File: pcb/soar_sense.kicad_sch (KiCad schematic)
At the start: 39 parts, among them J1 Conn_02x03_Top_Bottom, J2 Conn_02x02_Top_Bottom, J3 Conn_02x02_Top_Bottom, J4 Conn_02x02_Top_Bottom, J5 Conn_02x02_Top_Bottom, J6 Conn_02x01, J7 Conn_02x03_Top_Bottom, J8 Conn_02x04_Top_Bottom, U1 SPX3819M5-L-3-3, U2 STM32F103CBTx, U3 SHT35-DIS, U4 MAX3051, Y1 8MHz

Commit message: today done
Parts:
- removed J2: Conn_02x02_Top_Bottom, OWN_Parts:pcb_edge_2_2, symbol Connector_Generic:Conn_02x02_Top_Bottom
- added C15, C16, C17, C18, C19, C20: 100n, Capacitor_SMD:C_0603_1608Metric, symbol Device:C_Small
- added D10, D11, D12, D5, D6, D7, D8, D9: D_TVS, Diode_SMD:D_SOD-323, symbol Device:D_TVS
- added JP1: SolderJumper_2_Open, Jumper:SolderJumper-2_P1.3mm_Open_Pad1.0x1.5mm, symbol Jumper:SolderJumper_2_Open
- added R10, R11, R12, R13, R14, R15, R9: 10k, Resistor_SMD:R_0603_1608Metric, symbol Device:R_Small
- C10, C11, C12, C13, C14, C2, C6, C8, C9: LCSC Part Number (none) -> C14663
- C4: LCSC Part Number (none) -> C57112
- FB1: LCSC Part Number (none) -> C1017
- R1: LCSC Part Number (none) -> C25804
- R2: value 100k -> 120R; LCSC Part Number (none) -> C22787
- R4: value 100k -> 10k
- R5, R6: LCSC Part Number (none) -> C23162
- Y1: footprint (none) -> Crystal:Crystal_SMD_3225-4Pin_3.2x2.5mm
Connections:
- net +3V3: now also J1.2 (Pin_2), J1.3 (Pin_3); no longer J1.5 (Pin_5), J1.6 (Pin_6)
- net ADC_IN0: now also C19.1, R15.2; no longer J8.8 (Pin_8)
- net ADC_IN1: now also C16.1, R13.2; no longer J8.7 (Pin_7)
- net ADC_IN2: now also C17.1, R14.2; no longer J8.6 (Pin_6)
- net ADC_IN3: now also C15.1, R12.2; no longer J8.5 (Pin_5)
- net ADC_IN4: now also R4.2, C18.1; no longer J8.4 (Pin_4)
- net BOOT0: now also J1.1 (Pin_1), U2.44 (BOOT0), R9.2; no longer J1.3 (Pin_3), R4.2
- net BOOT1: now also U2.20 (PB2), R10.2; no longer J1.4 (Pin_4), R2.2
- net CAN_H: now also R2.1
- net CAN_L: now also JP1.2 (B)
- net GND: now also J1.4 (Pin_4), C15.2, C16.2, C17.2, C18.2, C19.2, C20.2, D10.1 (A1), D11.1 (A1), D12.1 (A1), D5.1 (A1), D6.1 (A1), D7.1 (A1), D8.1 (A1), D9.1 (A1), R10.1, R9.1; no longer J1.1 (Pin_1), J1.2 (Pin_2)
- net I2C1_SCL: now also D12.2 (A2)
- net I2C1_SDA: now also D11.2 (A2)
- net I2C2_SCL: now also D9.2 (A2)
- net I2C2_SDA: now also D10.2 (A2)
- net SPI2_MISO: now also D8.2 (A2)
- net SPI2_MOSI: now also D7.2 (A2)
- net SPI2_NSS: now also D5.2 (A2)
- net SPI2_SCK: now also D6.2 (A2)
- net USART1_RX: now also J1.5 (Pin_5)
- net USART1_TX: now also J1.6 (Pin_6)
- net VIN: now also D3.2 (A)
- net ADC_INPUT4: now reaches R4.1
- net ADC_INPUT4: now also J8.4 (Pin_4); no longer U2.44 (BOOT0)
- net ADC_INPUT5: now reaches J8.3 (Pin_3)
- net ADC_INPUT5: now also R11.1
- net ADC_IN5: now reaches U2.15 (PA5)
- net ADC_IN5: now also C20.1, R11.2
- new net: JP1.1 (A), R2.2
- new net ADC_INPUT0: J8.8 (Pin_8), R15.1
- new net ADC_INPUT1: J8.7 (Pin_7), R13.1
- new net ADC_INPUT2: J8.6 (Pin_6), R14.1
- new net ADC_INPUT3: J8.5 (Pin_5), R12.1
- no-connect marks 4 -> 15
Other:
- note added: "only overvoltage protection for adcs."
- note removed: "Input Protection"
- moved on the sheet: C14, J1, J3, J4, J5, J8, U4

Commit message: added crystal
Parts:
- removed R3: ??Ohm, Resistor_SMD:R_0603_1608Metric, symbol Device:R_Small
- C3, C5: value ??pF -> 30p; footprint Capacitor_SMD:C_0603_1608Metric -> Capacitor_SMD:C_0402_1005Metric; LCSC Part Number (none) -> C1570
- Y1: footprint Crystal:Crystal_SMD_3225-4Pin_3.2x2.5mm -> Crystal:Crystal_SMD_5032-4Pin_5.0x3.2mm; LCSC Part Number (none) -> C157341
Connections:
- net at C5.1, Y1.3: now also U2.6 (PD1)
- no-connect marks 15 -> 13
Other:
- note added: "CL = 2 * (Cload - Cstray)"
- moved on the sheet: C3, C5, Y1

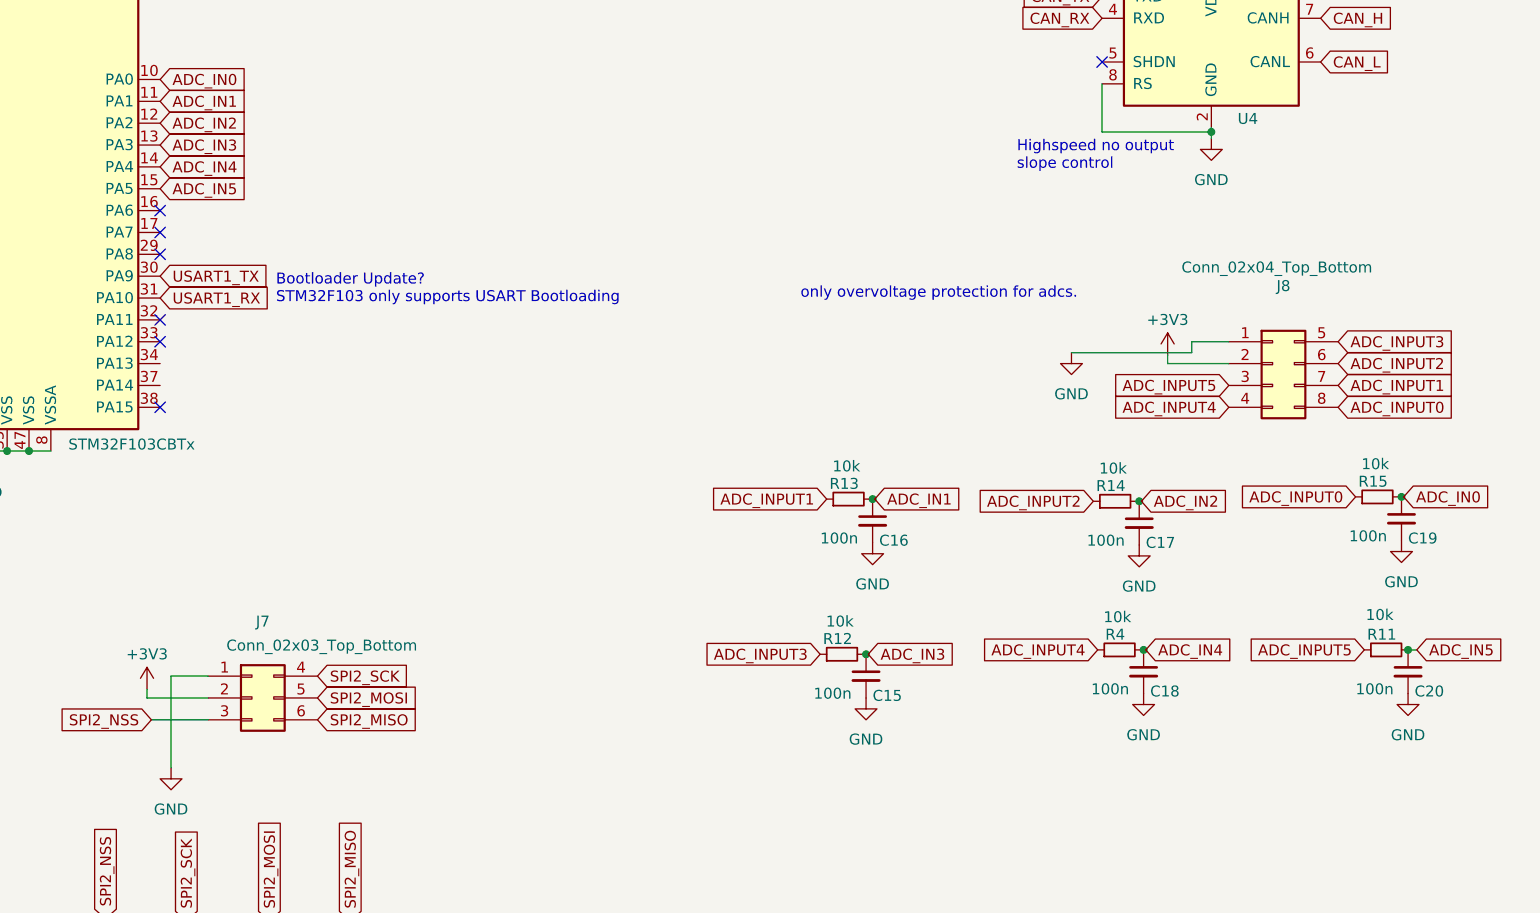
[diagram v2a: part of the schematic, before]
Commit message: sht connected
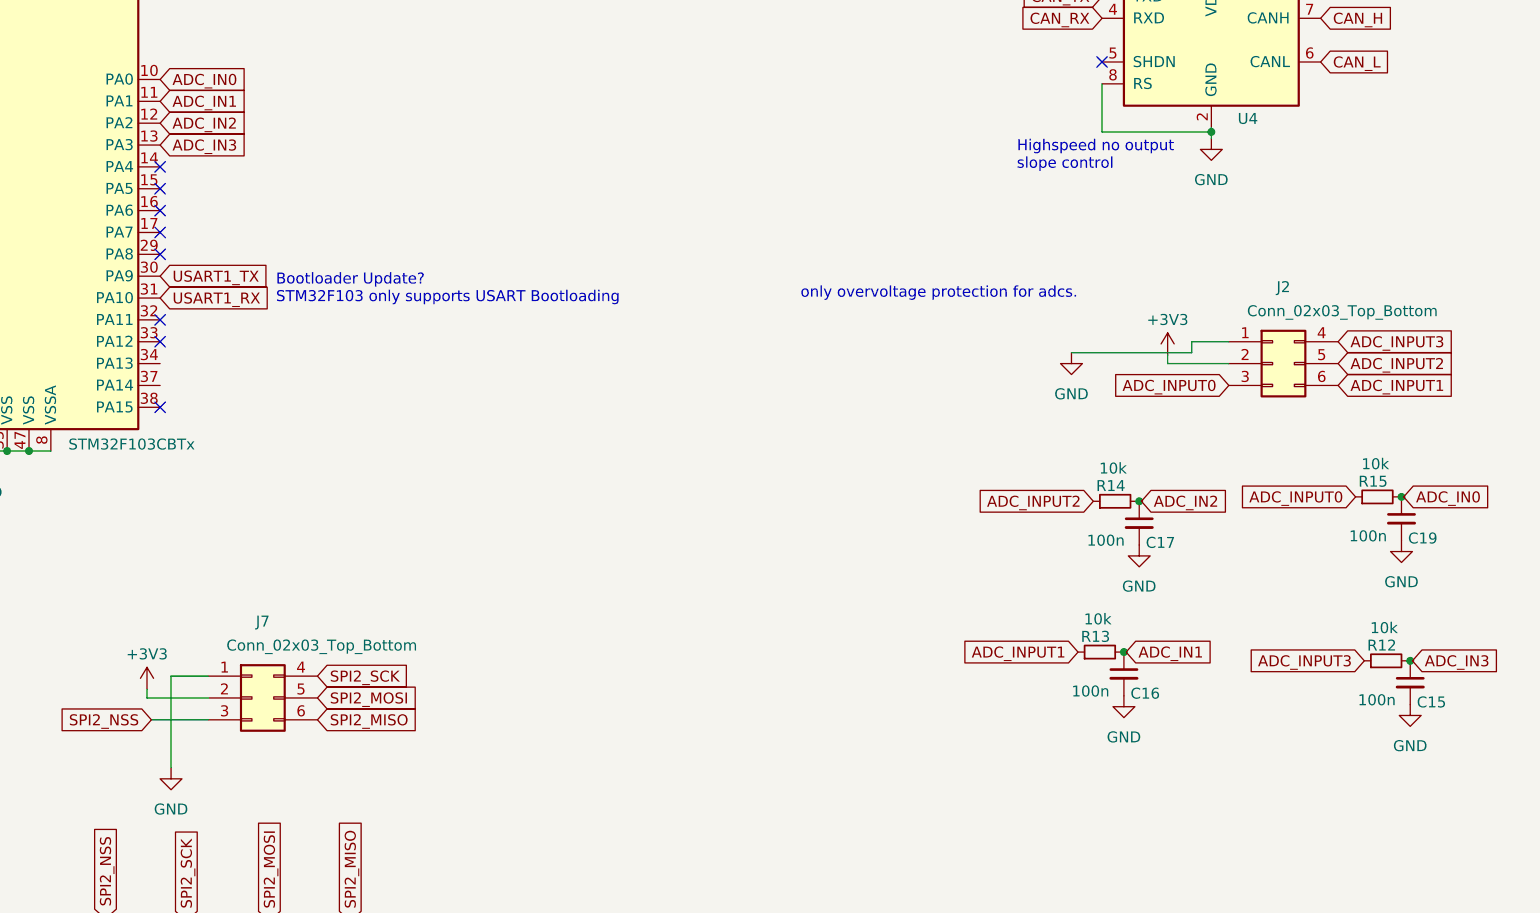
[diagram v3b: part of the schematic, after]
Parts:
- removed C18, C20: 100n, Capacitor_SMD:C_0603_1608Metric, symbol Device:C_Small
- removed J8: Conn_02x04_Top_Bottom, OWN_Parts:pcb_edge_2_4, symbol Connector_Generic:Conn_02x04_Top_Bottom
- removed R11, R4: 10k, Resistor_SMD:R_0603_1608Metric, symbol Device:R_Small
- added J2: Conn_02x03_Top_Bottom, OWN_Parts:pcb_edge_2_3, symbol Connector_Generic:Conn_02x03_Top_Bottom
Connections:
- net +3V3: now also J2.2 (Pin_2)
- net ADC_INPUT0: now also J2.3 (Pin_3)
- net ADC_INPUT1: now also J2.6 (Pin_6)
- net ADC_INPUT2: now also J2.5 (Pin_5)
- net ADC_INPUT3: now also J2.4 (Pin_4)
- net GND: now also J2.1 (Pin_1)
- net ADC_IN4: no longer names the net of U2.14 (PA4)
- net ADC_IN5: no longer names the net of U2.15 (PA5)
- no-connect marks 13 -> 15
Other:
- moved on the sheet: C15, C16, R12, R13

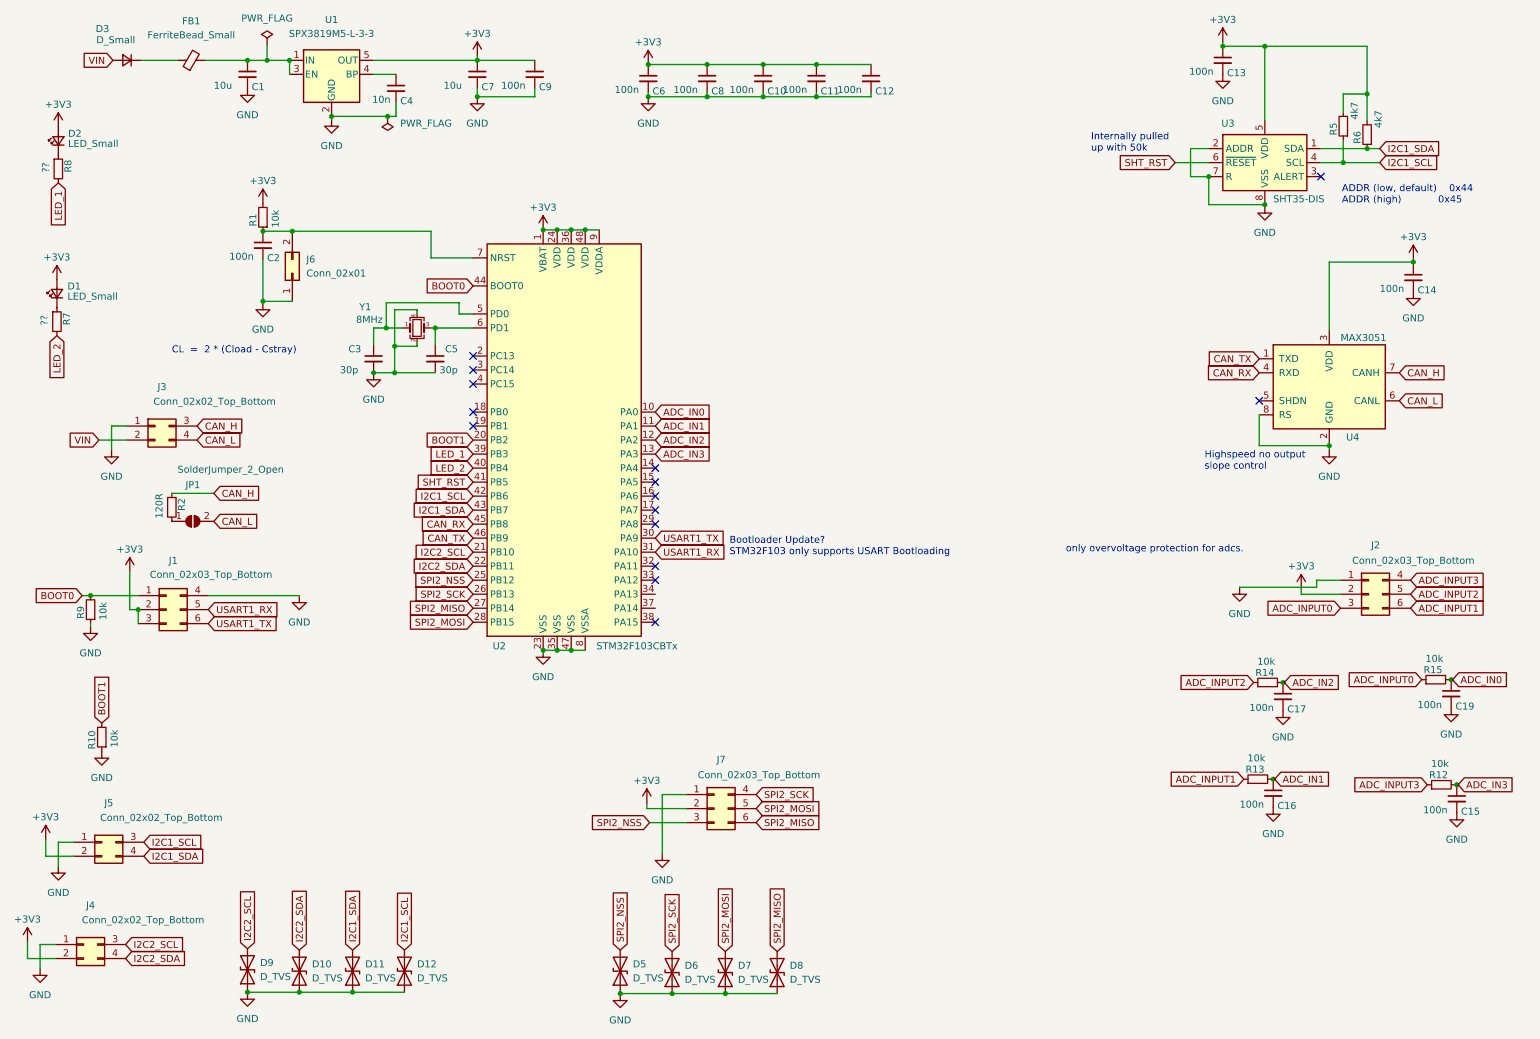
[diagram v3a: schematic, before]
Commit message: added copper heat cooling areas
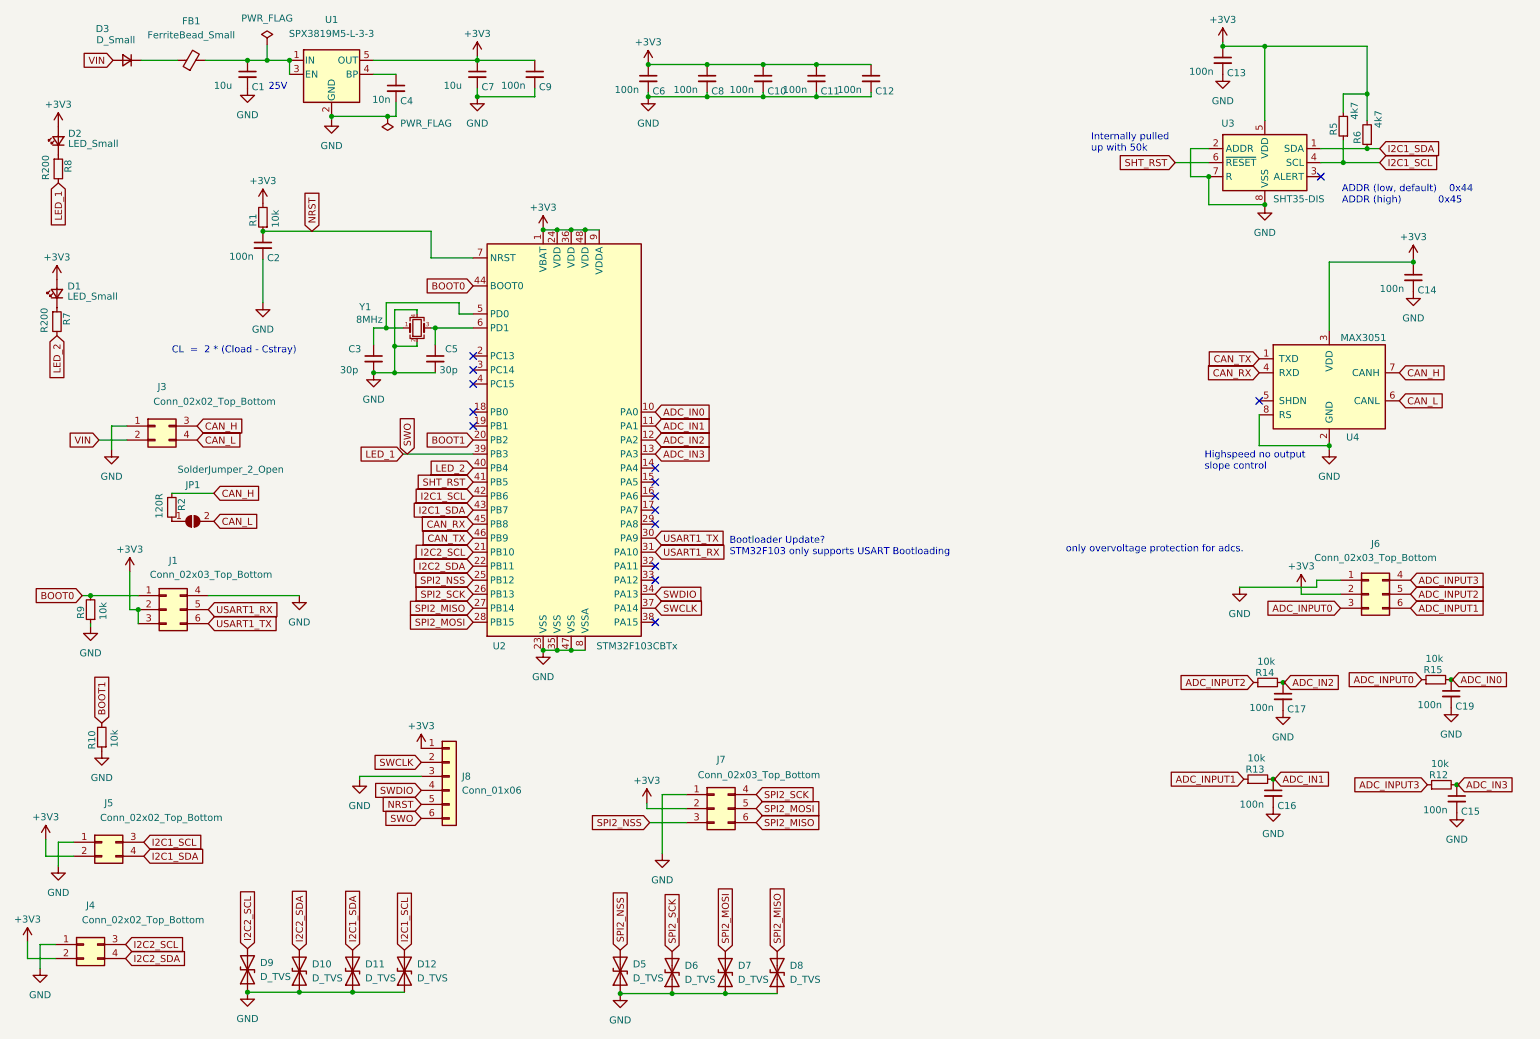
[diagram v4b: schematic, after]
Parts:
- removed J2: Conn_02x03_Top_Bottom, OWN_Parts:pcb_edge_2_3, symbol Connector_Generic:Conn_02x03_Top_Bottom
- removed J6: Conn_02x01, OWN_Parts:pcb_edge_2_1, symbol Connector_Generic:Conn_02x01
- added J6: Conn_02x03_Top_Bottom, OWN_Parts:pcb_edge_2_3, symbol Connector_Generic:Conn_02x03_Top_Bottom
- added J8: Conn_01x06, Connector_Molex:Molex_PicoBlade_53048-0610_1x06_P1.25mm_Horizontal, symbol Connector_Generic:Conn_01x06
- C1: LCSC Part Number (none) -> C91606
- C7: LCSC Part Number (none) -> C19702
- D1, D2: LCSC Part Number (none) -> C72041
- D3: footprint Diode_SMD:D_0603_1608Metric -> Diode_SMD:D_SOD-323; LCSC Part Number (none) -> C22624
- R12, R13, R14, R15: LCSC Part Number (none) -> C25804
- R7, R8: value ?? -> R200; LCSC Part Number (none) -> C8218
- U1: LCSC Part Number (none) -> C9055
- U2: LCSC Part Number (none) -> C8304
- U3: LCSC Part Number (none) -> C90161
- U4: footprint Package_TO_SOT_SMD:SOT-23-8 -> Package_TO_SOT_SMD:SOT-23-8_Handsoldering; LCSC Part Number (none) -> C112005
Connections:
- net +3V3: now also J6.2 (Pin_2), J8.1 (Pin_1)
- net ADC_INPUT0: now also J6.3 (Pin_3)
- net ADC_INPUT1: now also J6.6 (Pin_6)
- net ADC_INPUT2: now also J6.5 (Pin_5)
- net ADC_INPUT3: now also J6.4 (Pin_4)
- net GND: now also J6.1 (Pin_1), J8.3 (Pin_3)
- net LED_1: now also J8.6 (Pin_6)
- net SWDIO: now reaches U2.34 (PA13)
- net SWDIO: now also J8.4 (Pin_4)
- net SWCLK: now reaches U2.37 (PA14)
- net SWCLK: now also J8.2 (Pin_2)
- net NRST: now reaches C2.1, R1.1, U2.7 (NRST)
- net NRST: now also J8.5 (Pin_5)
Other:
- note added: "25V"

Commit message: added supply voltage sensing
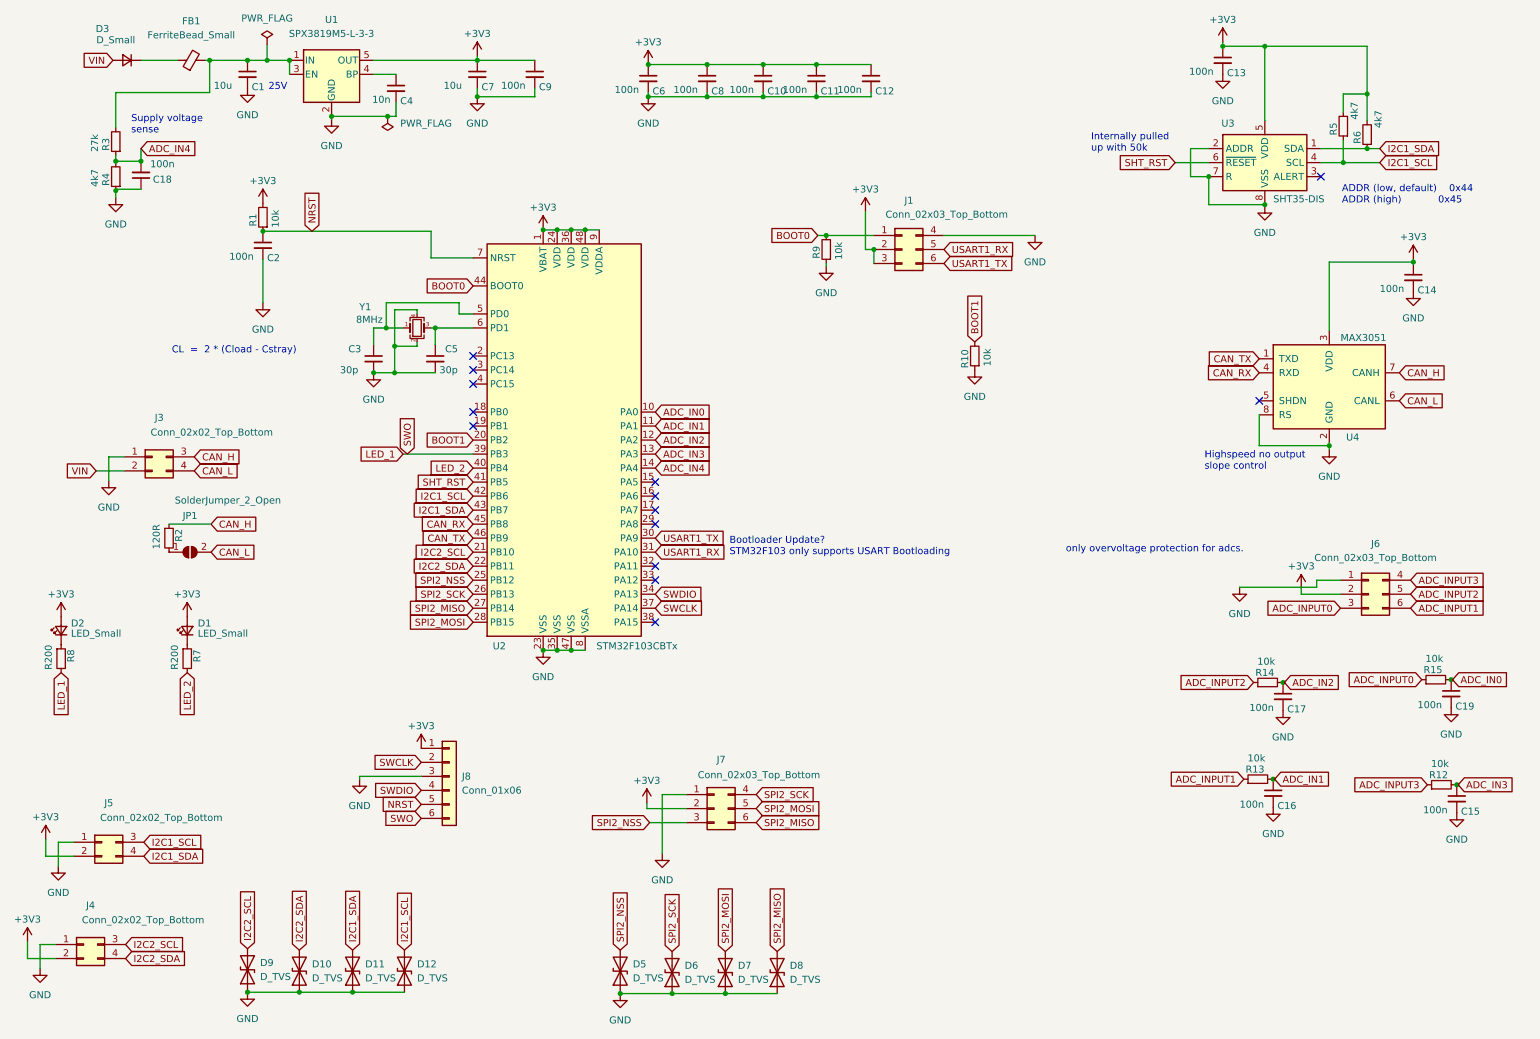
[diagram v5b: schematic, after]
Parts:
- added C18: 100n, Capacitor_SMD:C_0603_1608Metric, symbol Device:C_Small
- added R3: 27k, Resistor_SMD:R_0603_1608Metric, symbol Device:R_Small
- added R4: 4k7, Resistor_SMD:R_0603_1608Metric, symbol Device:R_Small
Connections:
- net GND: now also C18.1, R4.1
- net at C1.1, FB1.2, U1.1 (IN)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: now also R3.2
- net ADC_IN4: now reaches U2.14 (PA4)
- net ADC_IN4: now also C18.2, R3.1, R4.2
- no-connect marks 15 -> 14
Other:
- note added: "Supply voltage sense"
- moved on the sheet: D1, D2, J1, J3, JP1, R10, R2, R7, R8, R9

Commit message: updated documentation
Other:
- note added: "Analog inputs with overvoltage protection"
- note added: "CAN Transceiver"
- note added: "CAN connector with termination resistor jumper"
- note added: "Debug"
- note added: "I2C connectors with tvs protection"
- note added: "MCU decoupling"
- note added: "SPI connectors with tvs protection"
- note added: "Status LEDs"
- note added: "Temperature and Humidity sensing"
- note added: "UART and DFU flashing STM32F103 does not support DFU flashing via USB"
- note removed: "Bootloader Update? STM32F103 only supports USART Bootloading"
- note removed: "only overvoltage protection for adcs."
- title: (none) -> the SOAR SENSE
- moved on the sheet: C10, C11, C12, C6, C8, D1, D10, D11, D12, D2, D5, D6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
